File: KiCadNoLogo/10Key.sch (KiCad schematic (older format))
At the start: 57 parts, among them P1 USB_OTG, P2 Program, Q1 MMBT3906, Q2 MMBT3906, Q3 MMBT3906, Q4 MMBT3906, Q5 MMBT3906, SW1 SW_PUSH, SW10 5, SW11 2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

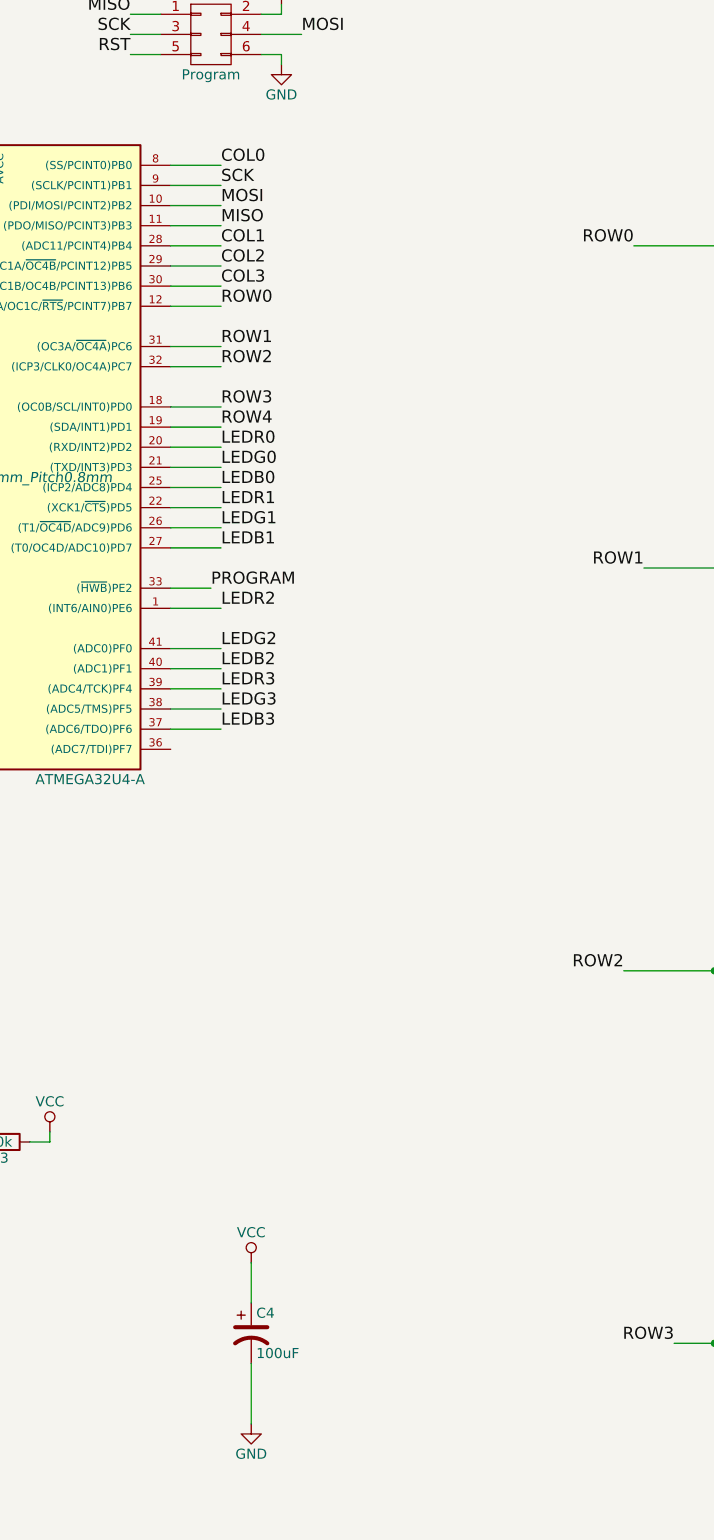
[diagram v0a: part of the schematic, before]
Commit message: Updated no logo pcb with current limiting resistors.
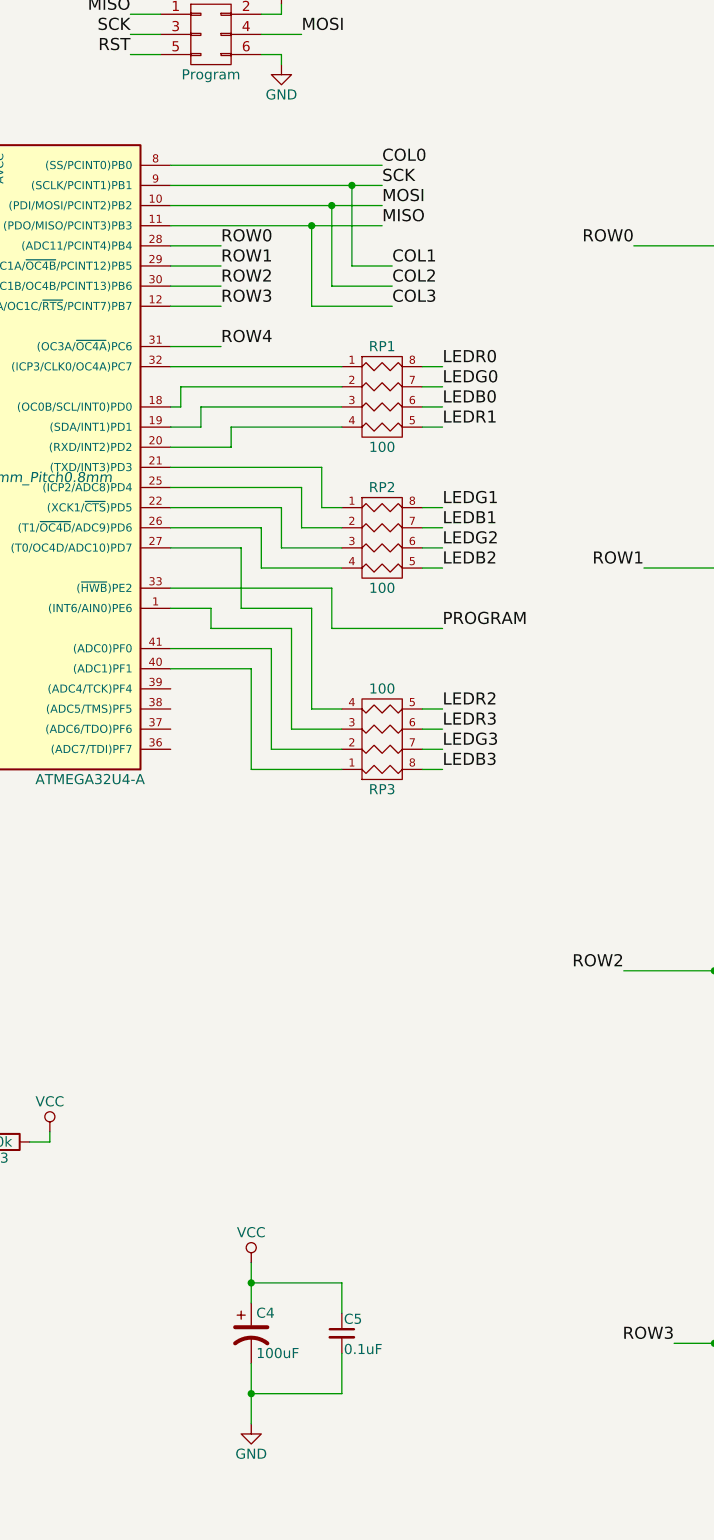
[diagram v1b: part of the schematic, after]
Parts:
- added C5: 0.1uF, Capacitors_SMD:C_0603_HandSoldering, symbol C_Small
- added RP1, RP2, RP3: 100, Resistors_SMD:R_Array_Convex_4x1206, symbol R_PACK4
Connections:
- net MISO is gone; now on net COL3: P2.1 (P1), U1.11 ((PDO/MISO/PCINT3)PB3)
- net MOSI is gone; now on net COL2: P2.4 (P4), U1.10 ((PDI/MOSI/PCINT2)PB2)
- net SCK is gone; now on net COL1: P2.3 (P3), U1.9 ((SCLK/PCINT1)PB1)
- net COL1: no longer U1.28 ((ADC11/PCINT4)PB4)
- net COL2: no longer U1.29 ((ADC12/OC1A/~OC4B~/PCINT12)PB5)
- net COL3: no longer U1.30 ((ADC13/OC1B/OC4B/PCINT13)PB6)
- net GND: now also C5.2
- net LEDB0: now also RP1.6 (R3); no longer U1.25 ((ICP2/ADC8)PD4)
- net LEDB1: now also RP2.7 (R2); no longer U1.27 ((T0/OC4D/ADC10)PD7)
- net LEDB2: now also RP2.5 (R4); no longer U1.40 ((ADC1)PF1)
- net LEDB3: now also RP3.8 (R1); no longer U1.37 ((ADC6/TDO)PF6)
- net LEDG0: now also RP1.7 (R2); no longer U1.21 ((TXD/INT3)PD3)
- net LEDG1: now also RP2.8 (R1); no longer U1.26 ((T1/~OC4D~/ADC9)PD6)
- net LEDG2: now also RP2.6 (R3); no longer U1.41 ((ADC0)PF0)
- net LEDG3: now also RP3.7 (R2); no longer U1.38 ((ADC5/TMS)PF5)
- net LEDR0: now also RP1.8 (R1); no longer U1.20 ((RXD/INT2)PD2)
- net LEDR1: now also RP1.5 (R4); no longer U1.22 ((XCK1/~CTS~)PD5)
- net LEDR2: now also RP3.5 (R4); no longer U1.1 ((INT6/AIN0)PE6)
- net LEDR3: now also RP3.6 (R3); no longer U1.39 ((ADC4/TCK)PF4)
- net ROW0: now also U1.28 ((ADC11/PCINT4)PB4); no longer U1.12 ((OC0A/OC1C/~RTS~/PCINT7)PB7)
- net ROW1: now also U1.29 ((ADC12/OC1A/~OC4B~/PCINT12)PB5); no longer U1.31 ((OC3A/~OC4A~)PC6)
- net ROW2: now also U1.30 ((ADC13/OC1B/OC4B/PCINT13)PB6); no longer U1.32 ((ICP3/CLK0/OC4A)PC7)
- net ROW3: now also U1.12 ((OC0A/OC1C/~RTS~/PCINT7)PB7); no longer U1.18 ((OC0B/SCL/INT0)PD0)
- net ROW4: now also U1.31 ((OC3A/~OC4A~)PC6); no longer U1.19 ((SDA/INT1)PD1)
- net VCC: now also C5.1
- new net: RP3.3 (P3), U1.1 ((INT6/AIN0)PE6)
- new net: RP1.2 (P2), U1.18 ((OC0B/SCL/INT0)PD0)
- new net: RP1.3 (P3), U1.19 ((SDA/INT1)PD1)
- new net: RP1.4 (P4), U1.20 ((RXD/INT2)PD2)
- new net: RP2.1 (P1), U1.21 ((TXD/INT3)PD3)
- new net: RP2.3 (P3), U1.22 ((XCK1/~CTS~)PD5)
- new net: RP2.2 (P2), U1.25 ((ICP2/ADC8)PD4)
- new net: RP2.4 (P4), U1.26 ((T1/~OC4D~/ADC9)PD6)
- new net: RP3.4 (P4), U1.27 ((T0/OC4D/ADC10)PD7)
- new net: RP1.1 (P1), U1.32 ((ICP3/CLK0/OC4A)PC7)
- new net: RP3.1 (P1), U1.40 ((ADC1)PF1)
- new net: RP3.2 (P2), U1.41 ((ADC0)PF0)
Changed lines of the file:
@@
 Text Label 2400 6300 2    60   ~ 0
 PROGRAM
-Text Label 4050 3550 0    60   ~ 0
+Text Label 5200 3750 0    60   ~ 0
 PROGRAM
-Text Label 4100 1550 0    60   ~ 0
+Text Label 4900 1550 0    60   ~ 0
 SCK
-Text Label 4100 1650 0    60   ~ 0
+Text Label 4900 1650 0    60   ~ 0
 MOSI
-Text Label 4100 1750 0    60   ~ 0
+Text Label 4900 1750 0    60   ~ 0
 MISO
-Wire Wire Line
-	3850 1550 4100 1550
-Wire Wire Line
-	3850 1650 4100 1650
-Wire Wire Line
-	3850 1750 4100 1750
 Text Label 1550 1200 1    60   ~ 0
 RST
@@
 	1550 1200 1550 1450
 Connection ~ 1550 1450
-Wire Wire Line
-	3850 3550 4050 3550
-Text Label 4100 1450 0    60   ~ 0
+Text Label 4900 1450 0    60   ~ 0
 COL0
-Text Label 4100 1850 0    60   ~ 0
+Text Label 4950 1950 0    60   ~ 0
 COL1
-Text Label 4100 1950 0    60   ~ 0
+Text Label 4950 2050 0    60   ~ 0
 COL2
-Text Label 4100 2050 0    60   ~ 0
+Text Label 4950 2150 0    60   ~ 0
 COL3
 $Comp
@@
 	1    0    0    -1
 $EndComp
+Text Label 4100 1850 0    60   ~ 0
+ROW0
+Text Label 4100 1950 0    60   ~ 0
+ROW1
+Text Label 4100 2050 0    60   ~ 0
+ROW2
 Text Label 4100 2150 0    60   ~ 0
-ROW0
+ROW3
 Text Label 4100 2350 0    60   ~ 0
-ROW1
-Text Label 4100 2450 0    60   ~ 0
-ROW2
-Text Label 4100 2650 0    60   ~ 0
-ROW3
-Text Label 4100 2750 0    60   ~ 0
 ROW4
-Text Label 4100 2850 0    60   ~ 0
+Text Label 5200 2450 0    60   ~ 0
 LEDR0
-Text Label 4100 2950 0    60   ~ 0
+Text Label 5200 2550 0    60   ~ 0
 LEDG0
-Text Label 4100 3050 0    60   ~ 0
+Text Label 5200 2650 0    60   ~ 0
 LEDB0
-Text Label 4100 3150 0    60   ~ 0
+Text Label 5200 2750 0    60   ~ 0
 LEDR1
-Text Label 4100 3250 0    60   ~ 0
+Text Label 5200 3150 0    60   ~ 0
 LEDG1
-Text Label 4100 3350 0    60   ~ 0
+Text Label 5200 3250 0    60   ~ 0
 LEDB1
-Text Label 4100 3650 0    60   ~ 0
+Text Label 5200 4150 0    60   ~ 0
 LEDR2
-Text Label 4100 3850 0    60   ~ 0
+Text Label 5200 3350 0    60   ~ 0
 LEDG2
-Text Label 4100 3950 0    60   ~ 0
+Text Label 5200 3450 0    60   ~ 0
 LEDB2
-Text Label 4100 4050 0    60   ~ 0
+Text Label 5200 4250 0    60   ~ 0
 LEDR3
-Text Label 4100 4150 0    60   ~ 0
+Text Label 5200 4350 0    60   ~ 0
 LEDG3
-Text Label 4100 4250 0    60   ~ 0
+Text Label 5200 4450 0    60   ~ 0
 LEDB3
-Wire Wire Line
-	3850 1850 4100 1850
-Wire Wire Line
-	3850 1950 4100 1950
-Wire Wire Line
-	3850 2050 4100 2050
-Wire Wire Line
-	3850 2150 4100 2150
-Wire Wire Line
-	3850 2350 4100 2350
-Wire Wire Line
-	3850 2450 4100 2450
-Wire Wire Line
-	3850 2650 4100 2650
-Wire Wire Line
-	3850 2750 4100 2750
-Wire Wire Line
-	3850 2850 4100 2850
-Wire Wire Line
-	3850 2950 4100 2950
-Wire Wire Line
-	3850 3050 4100 3050
-Wire Wire Line
-	3850 3150 4100 3150
-Wire Wire Line
-	3850 3250 4100 3250
-Wire Wire Line
-	3850 3350 4100 3350
-Wire Wire Line
-	3850 3650 4100 3650
-Wire Wire Line
-	3850 3850 4100 3850
-Wire Wire Line
-	3850 3950 4100 3950
-Wire Wire Line
-	3850 4050 4100 4050
-Wire Wire Line
-	3850 4150 4100 4150
-Wire Wire Line
-	3850 4250 4100 4250
-Wire Wire Line
-	3850 1450 4100 1450
 $Comp
 L MMBT3906 Q3
@@
 Wire Wire Line
 	4250 7400 4250 7700
+Wire Wire Line
+	4900 1450 3850 1450
+Wire Wire Line
+	3850 1550 4900 1550
+Wire Wire Line
+	4750 1550 4750 1950
+Wire Wire Line
+	4750 1950 4950 1950
+Connection ~ 4750 1550
+Wire Wire Line
+	3850 1650 4900 1650
+Wire Wire Line
+	3850 1750 4900 1750
+Wire Wire Line
+	4650 1650 4650 2050
+Wire Wire Line
+	4650 2050 4950 2050
+Connection ~ 4650 1650
+Wire Wire Line
+	4550 1750 4550 2150
+Wire Wire Line
+	4550 2150 4950 2150
+Connection ~ 4550 1750
+Wire Wire Line
+	3850 1850 4100 1850
+Wire Wire Line
+	3850 1950 4100 1950
+Wire Wire Line
+	3850 2050 4100 2050
+Wire Wire Line
+	3850 2150 4100 2150
+Wire Wire Line
+	3850 2350 4100 2350
+$Comp
+L R_PACK4 RP1
+U 1 1 57A2C523
+P 4900 2800
+F 0 "RP1" H 4900 3250 50  0000 C CNN
+F 1 "100" H 4900 2750 50  0000 C CNN
+F 2 "Resistors_SMD:R_Array_Convex_4x1206" H 4900 2800 50  0001 C CNN
+F 3 "" H 4900 2800 50  0000 C CNN
+	1    4900 2800
+	1    0    0    -1
+$EndComp
+$Comp
+L R_PACK4 RP2
+U 1 1 57A2C672
+P 4900 3500
+F 0 "RP2" H 4900 3950 50  0000 C CNN
+F 1 "100" H 4900 3450 50  0000 C CNN
+F 2 "Resistors_SMD:R_Array_Convex_4x1206" H 4900 3500 50  0001 C CNN
+F 3 "" H 4900 3500 50  0000 C CNN
+	1    4900 3500
+	1    0    0    -1
+$EndComp
+$Comp
+L R_PACK4 RP3
+U 1 1 57A2C707
+P 4900 4100
+F 0 "RP3" H 4900 4550 50  0000 C CNN
+F 1 "100" H 4900 4050 50  0000 C CNN
+F 2 "Resistors_SMD:R_Array_Convex_4x1206" H 4900 4100 50  0001 C CNN
+F 3 "" H 4900 4100 50  0000 C CNN
+	1    4900 4100
+	1    0    0    1
+$EndComp
+Wire Wire Line
+	3850 2450 4700 2450
+Wire Wire Line
+	3850 2650 3900 2650
+Wire Wire Line
+	3900 2650 3900 2550
+Wire Wire Line
+	3900 2550 4700 2550
+Wire Wire Line
+	3850 2750 4000 2750
+Wire Wire Line
+	4000 2750 4000 2650
+Wire Wire Line
+	4000 2650 4700 2650
+Wire Wire Line
+	3850 2850 4150 2850
+Wire Wire Line
+	4150 2850 4150 2750
+Wire Wire Line
+	4150 2750 4700 2750
+Wire Wire Line
+	3850 2950 4600 2950
+Wire Wire Line
+	4600 2950 4600 3150
+Wire Wire Line
+	4600 3150 4700 3150
+Wire Wire Line
+	3850 3050 4500 3050
+Wire Wire Line
+	4500 3050 4500 3250
+Wire Wire Line
+	4500 3250 4700 3250
+Wire Wire Line
+	3850 3150 4400 3150
+Wire Wire Line
+	4400 3150 4400 3350
+Wire Wire Line
+	4400 3350 4700 3350
+Wire Wire Line
+	3850 3250 4300 3250
+Wire Wire Line
+	4300 3250 4300 3450
+Wire Wire Line
+	4300 3450 4700 3450
+Wire Wire Line
+	3850 3350 4200 3350
+Wire Wire Line
+	4200 3350 4200 3650
+Wire Wire Line
+	4200 3650 4550 3650
+Wire Wire Line
+	4550 3650 4550 4150
+Wire Wire Line
+	3850 3650 4050 3650
+Wire Wire Line
+	4050 3650 4050 3750
+Wire Wire Line
+	4050 3750 4450 3750
+Wire Wire Line
+	4450 3750 4450 4250
+Wire Wire Line
+	3850 3850 4350 3850
+Wire Wire Line
+	4350 3850 4350 4350
+Wire Wire Line
+	3850 3950 4250 3950
+Wire Wire Line
+	4250 3950 4250 4450
+Wire Wire Line
+	3850 3550 4650 3550
+Wire Wire Line
+	4650 3550 4650 3750
+Wire Wire Line
+	4650 3750 5200 3750
+Wire Wire Line
+	5100 3150 5200 3150
+Wire Wire Line
+	5100 3250 5200 3250
+Wire Wire Line
+	5100 3350 5200 3350
+Wire Wire Line
+	5100 3450 5200 3450
+$Comp
+L C_Small C5
+U 1 1 57A303BA
+P 4700 7250
+F 0 "C5" H 4710 7320 50  0000 L CNN
+F 1 "0.1uF" H 4710 7170 50  0000 L CNN
+F 2 "Capacitors_SMD:C_0603_HandSoldering" H 4700 7250 50  0001 C CNN
+F 3 "" H 4700 7250 50  0000 C CNN
+	1    4700 7250
+	1    0    0    -1
+$EndComp
+Wire Wire Line
+	4250 7000 4700 7000
+Wire Wire Line
+	4700 7000 4700 7150
+Connection ~ 4250 7000
+Wire Wire Line
+	4700 7350 4700 7550
+Wire Wire Line
+	4700 7550 4250 7550
+Connection ~ 4250 7550
+Wire Wire Line
+	5100 2450 5200 2450
+Wire Wire Line
+	5100 2550 5200 2550
+Wire Wire Line
+	5100 2650 5200 2650
+Wire Wire Line
+	5100 2750 5200 2750
+Wire Wire Line
+	4550 4150 4700 4150
+Wire Wire Line
+	5100 4150 5200 4150
+Wire Wire Line
+	5100 4250 5200 4250
+Wire Wire Line
+	5100 4350 5200 4350
+Wire Wire Line
+	5100 4450 5200 4450
+Wire Wire Line
+	4450 4250 4700 4250
+Wire Wire Line
+	4350 4350 4700 4350
+Wire Wire Line
+	4250 4450 4700 4450
 $EndSCHEMATC
